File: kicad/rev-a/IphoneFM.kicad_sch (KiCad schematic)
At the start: 0 parts

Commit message: Step 1.4: U1 STM32U535CEUx placed; all 49 pins match netlist.json
Co-Authored-By: Claude Opus 5.5 <noreply@anthropic.com>
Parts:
- added U1: STM32U535CEU6, Package_DFN_QFN:QFN-48-1EP_7x7mm_P0.5mm_EP5.6x5.6mm, symbol MCU_ST_STM32U5:STM32U535CEUx
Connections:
- new net: U1.23 (VSS), U1.35 (VSS), U1.47 (VSS), U1.49 (VSS)
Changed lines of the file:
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@@
 		(comment 2 "Source of truth: design/rev-a/netlist.json")
+	)
+	(symbol
+		(lib_id "MCU_ST_STM32U5:STM32U535CEUx")
+		(at 223.52 251.46 0)
+		(unit 1)
+		(exclude_from_sim no)
+		(in_bom yes)
+		(on_board yes)
+		(dnp no)
+		(property "Reference" "U1"
+			(at 223.52 247.65 0)
+			(effects (font (size 1.27 1.27)))
+		)
+		(property "Value" "STM32U535CEU6"
+			(at 223.52 255.27 0)
+			(effects (font (size 1.27 1.27)))
+		)
+		(property "Footprint" "Package_DFN_QFN:QFN-48-1EP_7x7mm_P0.5mm_EP5.6x5.6mm"
+			(at 223.52 251.46 0)
+			(effects (font (size 1.27 1.27)) (hide yes))
+		)
+		(property "Datasheet" "~"
+			(at 223.52 251.46 0)
+			(effects (font (size 1.27 1.27)) (hide yes))
+		)
+		(instances
+			(project "IphoneFM"
+				(path "/efee88c9-028d-4fdb-86e0-0a4145b330e1"
+					(reference "U1") (unit 1)
+				)
+			)
+		)
 	)
 	(sheet_instances

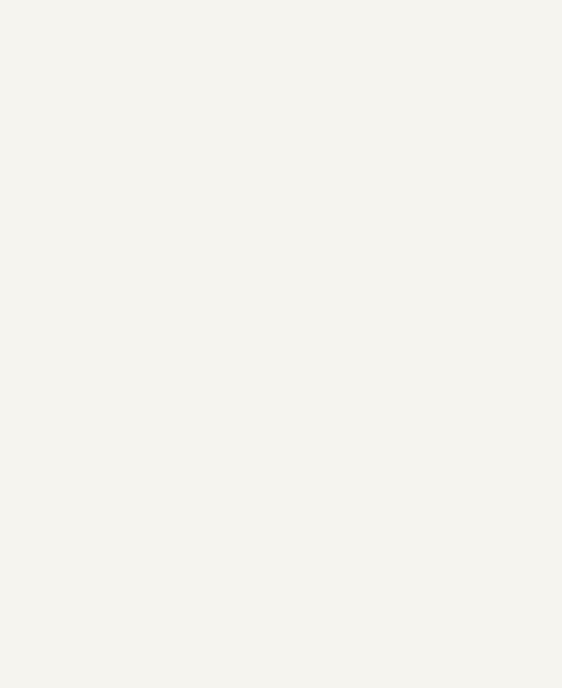
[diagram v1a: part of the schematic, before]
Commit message: Step 1.5: U2 LMX2571 placed from a project symbol built from SNAS654A p3-4 (tools/kicad_symbol.py)
Co-Authored-By: Claude Opus 5.5 <noreply@anthropic.com>
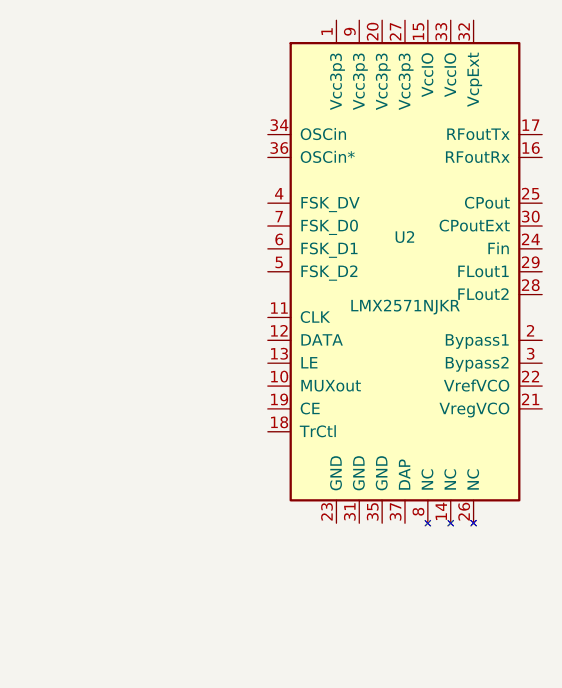
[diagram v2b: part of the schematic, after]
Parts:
- added U2: LMX2571NJKR, symbol IphoneFM:LMX2571
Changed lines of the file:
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@@
+		)
+	)
+	(symbol
+		(lib_id "IphoneFM:LMX2571")
+		(at 337.82 88.9 0)
+		(unit 1)
+		(exclude_from_sim no)
+		(in_bom yes)
+		(on_board yes)
+		(dnp no)
+		(property "Reference" "U2"
+			(at 337.82 85.09 0)
+			(effects (font (size 1.27 1.27)))
+		)
+		(property "Value" "LMX2571NJKR"
+			(at 337.82 92.71 0)
+			(effects (font (size 1.27 1.27)))
+		)
+		(property "Footprint" ""
+			(at 337.82 88.9 0)
+			(effects (font (size 1.27 1.27)) (hide yes))
+		)
+		(property "Datasheet" "~"
+			(at 337.82 88.9 0)
+			(effects (font (size 1.27 1.27)) (hide yes))
+		)
+		(instances
+			(project "IphoneFM"
+				(path "/efee88c9-028d-4fdb-86e0-0a4145b330e1"
+					(reference "U2") (unit 1)
+				)
+			)
 		)
 	)

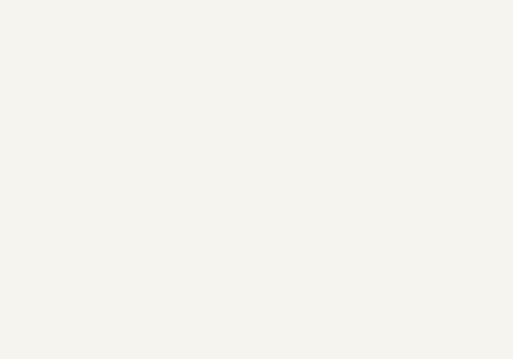
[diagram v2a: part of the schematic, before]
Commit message: Step 1.6: U3 AP2112K-3.3 placed (KiCad library symbol, 5/5 pins match)
Co-Authored-By: Claude Opus 5.5 <noreply@anthropic.com>
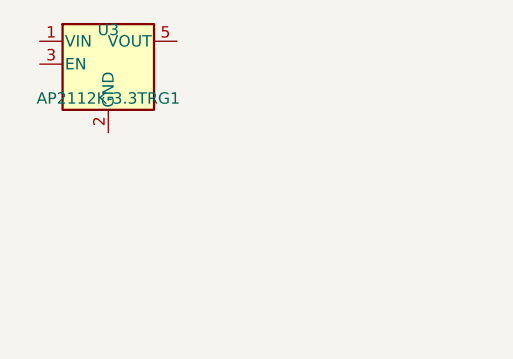
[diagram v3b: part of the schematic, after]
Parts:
- added U3: AP2112K-3.3TRG1, Package_TO_SOT_SMD:SOT-23-5, symbol Regulator_Linear:AP2112K-3.3
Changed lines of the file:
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@@
+		)
+	)
+	(symbol
+		(lib_id "Regulator_Linear:AP2112K-3.3")
+		(at 120.65 45.72 0)
+		(unit 1)
+		(exclude_from_sim no)
+		(in_bom yes)
+		(on_board yes)
+		(dnp no)
+		(property "Reference" "U3"
+			(at 120.65 41.91 0)
+			(effects (font (size 1.27 1.27)))
+		)
+		(property "Value" "AP2112K-3.3TRG1"
+			(at 120.65 49.53 0)
+			(effects (font (size 1.27 1.27)))
+		)
+		(property "Footprint" "Package_TO_SOT_SMD:SOT-23-5"
+			(at 120.65 45.72 0)
+			(effects (font (size 1.27 1.27)) (hide yes))
+		)
+		(property "Datasheet" "~"
+			(at 120.65 45.72 0)
+			(effects (font (size 1.27 1.27)) (hide yes))
+		)
+		(instances
+			(project "IphoneFM"
+				(path "/efee88c9-028d-4fdb-86e0-0a4145b330e1"
+					(reference "U3") (unit 1)
+				)
+			)
 		)
 	)

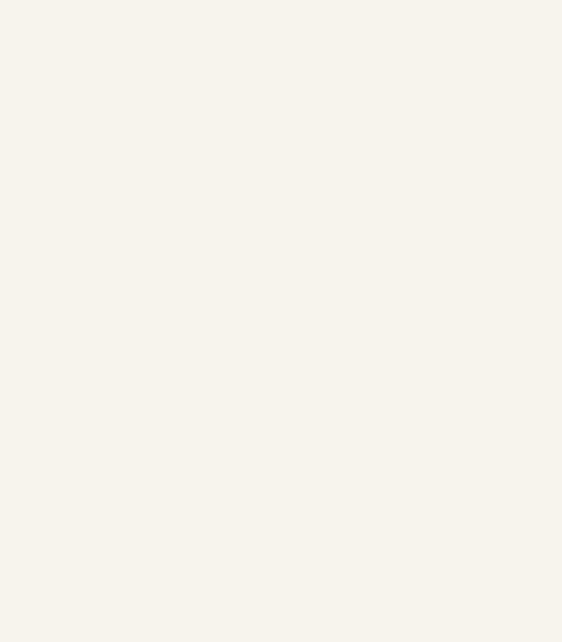
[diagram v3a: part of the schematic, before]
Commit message: Step 1.7: U4 Si4705-D60-GM placed from a project symbol (QFN-20, datasheet p16)
Co-Authored-By: Claude Opus 5.5 <noreply@anthropic.com>
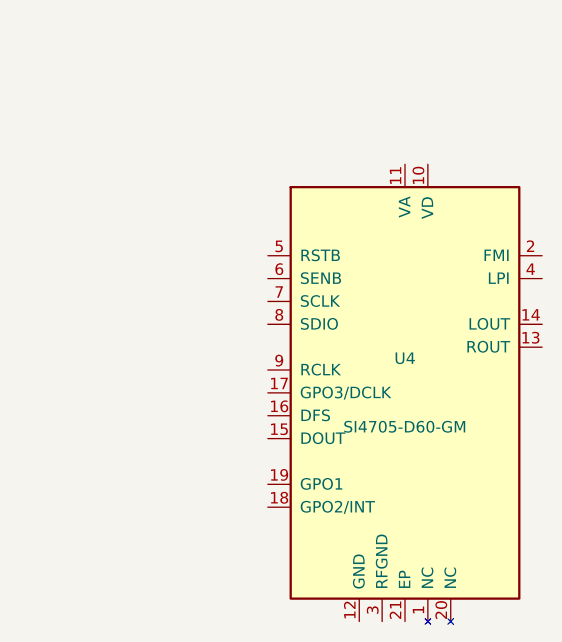
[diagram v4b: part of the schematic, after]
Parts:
- added U4: SI4705-D60-GM, symbol IphoneFM:Si4705-D60-GM
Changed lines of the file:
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@@
+		)
+	)
+	(symbol
+		(lib_id "IphoneFM:Si4705-D60-GM")
+		(at 365.76 304.8 0)
+		(unit 1)
+		(exclude_from_sim no)
+		(in_bom yes)
+		(on_board yes)
+		(dnp no)
+		(property "Reference" "U4"
+			(at 365.76 300.99 0)
+			(effects (font (size 1.27 1.27)))
+		)
+		(property "Value" "SI4705-D60-GM"
+			(at 365.76 308.61 0)
+			(effects (font (size 1.27 1.27)))
+		)
+		(property "Footprint" ""
+			(at 365.76 304.8 0)
+			(effects (font (size 1.27 1.27)) (hide yes))
+		)
+		(property "Datasheet" "~"
+			(at 365.76 304.8 0)
+			(effects (font (size 1.27 1.27)) (hide yes))
+		)
+		(instances
+			(project "IphoneFM"
+				(path "/efee88c9-028d-4fdb-86e0-0a4145b330e1"
+					(reference "U4") (unit 1)
+				)
+			)
 		)
 	)

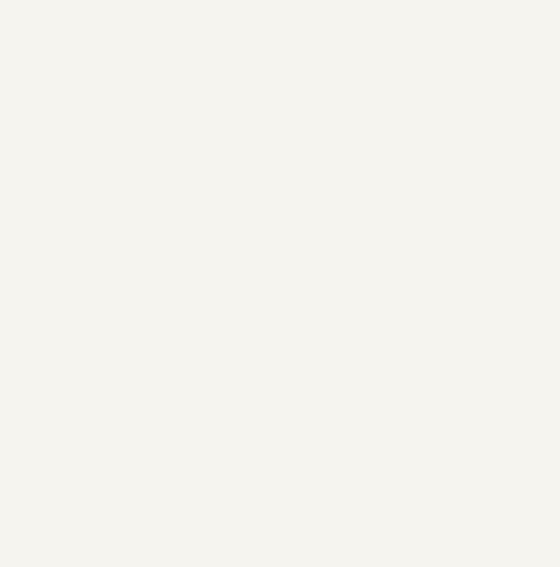
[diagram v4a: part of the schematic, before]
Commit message: Step 1.8: U5 PE42421 placed from a project symbol (p8)
Co-Authored-By: Claude Opus 5.5 <noreply@anthropic.com>
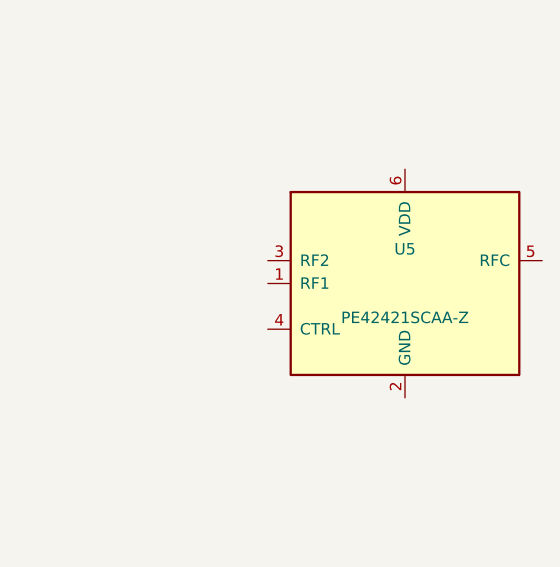
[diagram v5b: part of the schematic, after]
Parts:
- added U5: PE42421SCAA-Z, symbol IphoneFM:PE42421
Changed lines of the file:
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@@
+		)
+	)
+	(symbol
+		(lib_id "IphoneFM:PE42421")
+		(at 520.7 152.4 0)
+		(unit 1)
+		(exclude_from_sim no)
+		(in_bom yes)
+		(on_board yes)
+		(dnp no)
+		(property "Reference" "U5"
+			(at 520.7 148.59 0)
+			(effects (font (size 1.27 1.27)))
+		)
+		(property "Value" "PE42421SCAA-Z"
+			(at 520.7 156.21 0)
+			(effects (font (size 1.27 1.27)))
+		)
+		(property "Footprint" ""
+			(at 520.7 152.4 0)
+			(effects (font (size 1.27 1.27)) (hide yes))
+		)
+		(property "Datasheet" "~"
+			(at 520.7 152.4 0)
+			(effects (font (size 1.27 1.27)) (hide yes))
+		)
+		(instances
+			(project "IphoneFM"
+				(path "/efee88c9-028d-4fdb-86e0-0a4145b330e1"
+					(reference "U5") (unit 1)
+				)
+			)
 		)
 	)

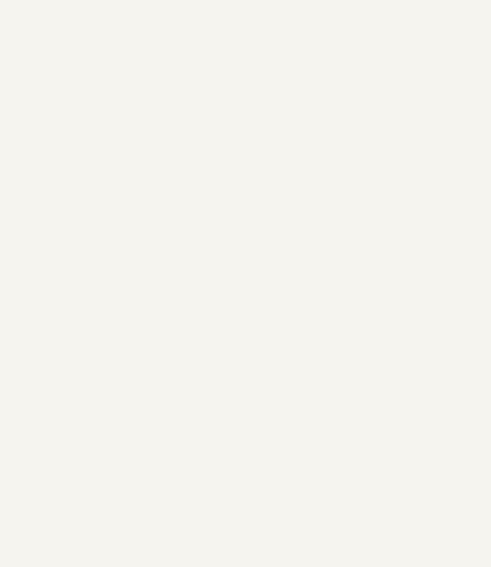
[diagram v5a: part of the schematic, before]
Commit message: Step 1.9: U6 USBLC6-2SC6 placed (KiCad library symbol, 6/6 pins match)
Co-Authored-By: Claude Opus 5.5 <noreply@anthropic.com>
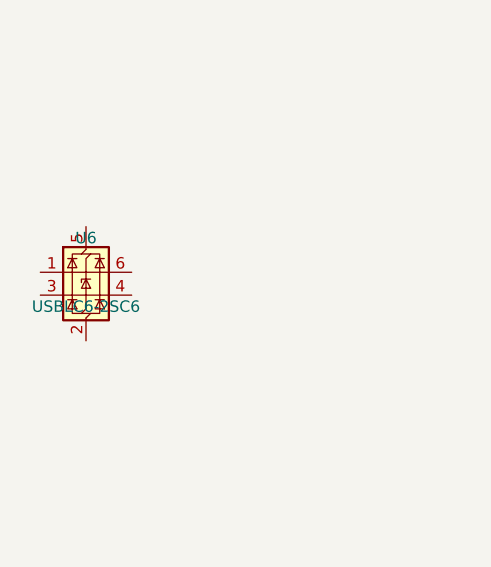
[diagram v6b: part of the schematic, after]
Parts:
- added U6: USBLC6-2SC6, Package_TO_SOT_SMD:SOT-23-6, symbol Power_Protection:USBLC6-2SC6
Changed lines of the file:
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@@
+		)
+	)
+	(symbol
+		(lib_id "Power_Protection:USBLC6-2SC6")
+		(at 73.66 93.98 0)
+		(unit 1)
+		(exclude_from_sim no)
+		(in_bom yes)
+		(on_board yes)
+		(dnp no)
+		(property "Reference" "U6"
+			(at 73.66 90.17 0)
+			(effects (font (size 1.27 1.27)))
+		)
+		(property "Value" "USBLC6-2SC6"
+			(at 73.66 97.79 0)
+			(effects (font (size 1.27 1.27)))
+		)
+		(property "Footprint" "Package_TO_SOT_SMD:SOT-23-6"
+			(at 73.66 93.98 0)
+			(effects (font (size 1.27 1.27)) (hide yes))
+		)
+		(property "Datasheet" "~"
+			(at 73.66 93.98 0)
+			(effects (font (size 1.27 1.27)) (hide yes))
+		)
+		(instances
+			(project "IphoneFM"
+				(path "/efee88c9-028d-4fdb-86e0-0a4145b330e1"
+					(reference "U6") (unit 1)
+				)
+			)
 		)
 	)

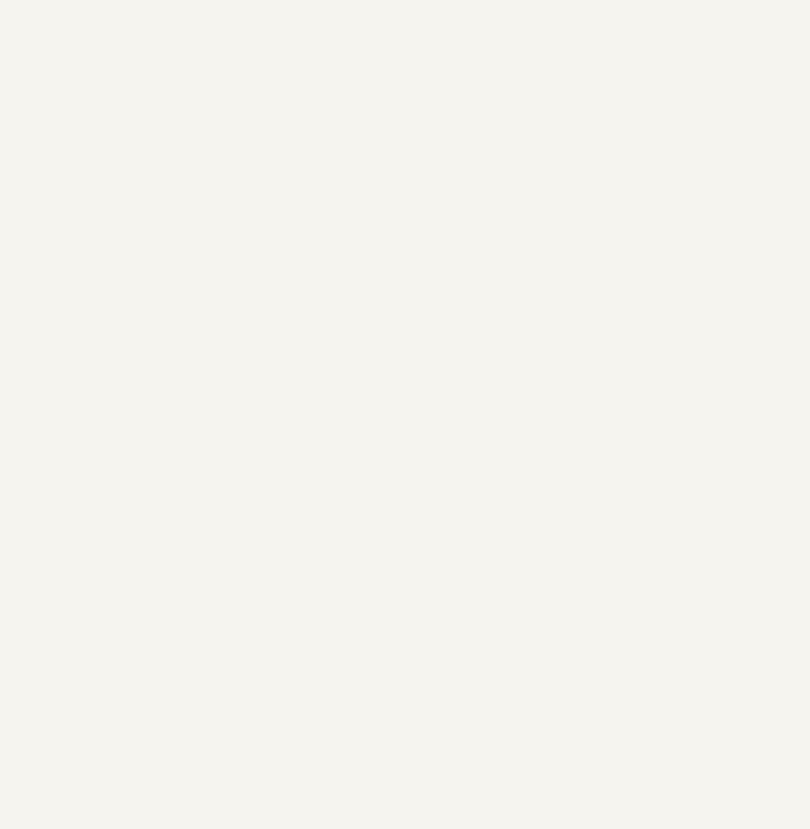
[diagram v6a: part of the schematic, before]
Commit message: Step 1.10: U7 PE43711 placed from a project symbol (Table 9 p28)
Co-Authored-By: Claude Opus 5.5 <noreply@anthropic.com>
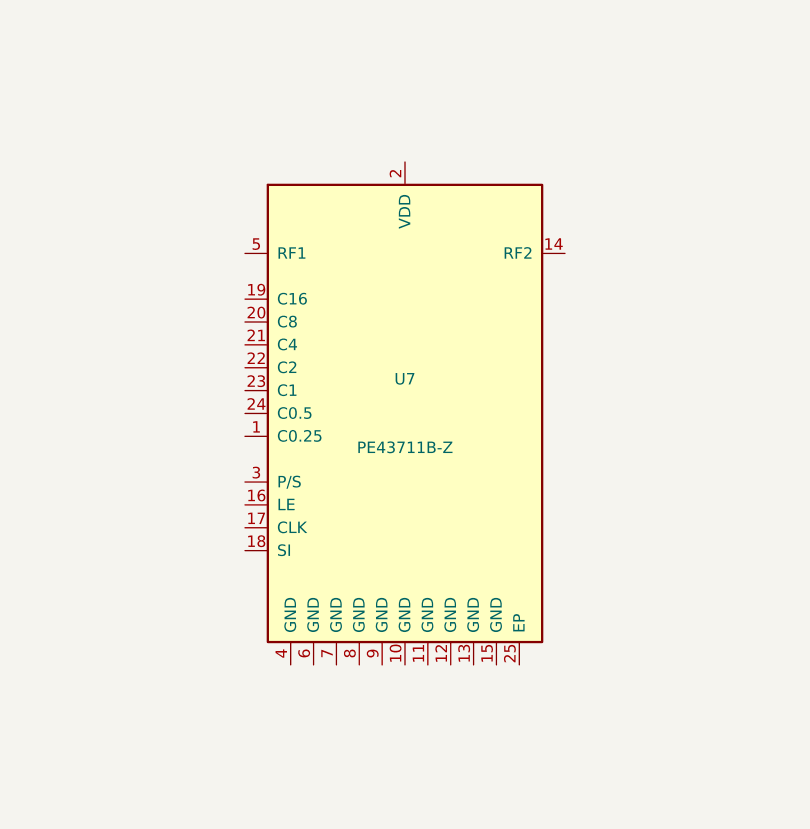
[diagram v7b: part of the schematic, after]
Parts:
- added U7: PE43711B-Z, symbol IphoneFM:PE43711
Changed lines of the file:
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@@
+		)
+	)
+	(symbol
+		(lib_id "IphoneFM:PE43711")
+		(at 406.4 101.6 0)
+		(unit 1)
+		(exclude_from_sim no)
+		(in_bom yes)
+		(on_board yes)
+		(dnp no)
+		(property "Reference" "U7"
+			(at 406.4 97.79 0)
+			(effects (font (size 1.27 1.27)))
+		)
+		(property "Value" "PE43711B-Z"
+			(at 406.4 105.41 0)
+			(effects (font (size 1.27 1.27)))
+		)
+		(property "Footprint" ""
+			(at 406.4 101.6 0)
+			(effects (font (size 1.27 1.27)) (hide yes))
+		)
+		(property "Datasheet" "~"
+			(at 406.4 101.6 0)
+			(effects (font (size 1.27 1.27)) (hide yes))
+		)
+		(instances
+			(project "IphoneFM"
+				(path "/efee88c9-028d-4fdb-86e0-0a4145b330e1"
+					(reference "U7") (unit 1)
+				)
+			)
 		)
 	)

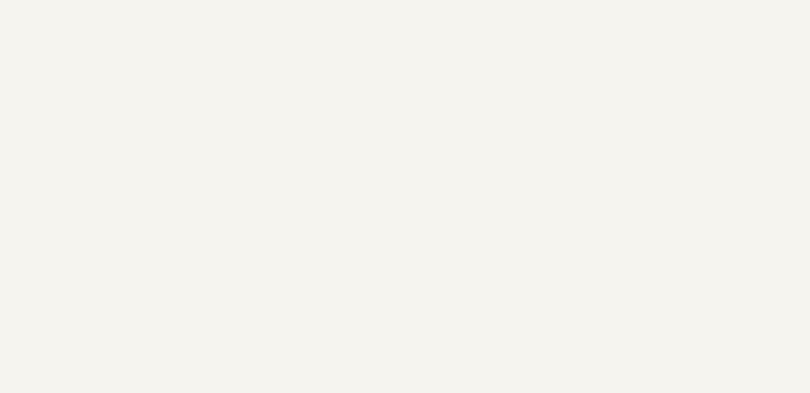
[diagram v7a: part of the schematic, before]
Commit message: Step 1.11: Y2 OT322520MJBA4SL 20 MHz placed from a project symbol (YSO110TR p2)
Co-Authored-By: Claude Opus 5.5 <noreply@anthropic.com>
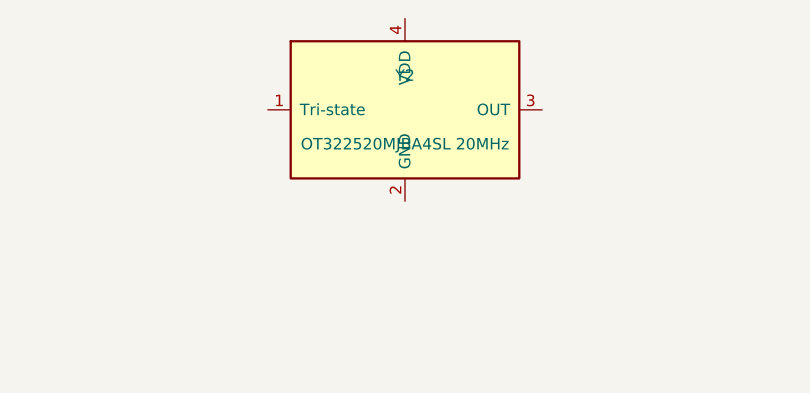
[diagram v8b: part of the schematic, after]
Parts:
- added Y2: OT322520MJBA4SL 20MHz, symbol IphoneFM:OT322520MJBA4SL
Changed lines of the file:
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@@
+		)
+	)
+	(symbol
+		(lib_id "IphoneFM:OT322520MJBA4SL")
+		(at 223.52 50.8 0)
+		(unit 1)
+		(exclude_from_sim no)
+		(in_bom yes)
+		(on_board yes)
+		(dnp no)
+		(property "Reference" "Y2"
+			(at 223.52 46.99 0)
+			(effects (font (size 1.27 1.27)))
+		)
+		(property "Value" "OT322520MJBA4SL 20MHz"
+			(at 223.52 54.61 0)
+			(effects (font (size 1.27 1.27)))
+		)
+		(property "Footprint" ""
+			(at 223.52 50.8 0)
+			(effects (font (size 1.27 1.27)) (hide yes))
+		)
+		(property "Datasheet" "~"
+			(at 223.52 50.8 0)
+			(effects (font (size 1.27 1.27)) (hide yes))
+		)
+		(instances
+			(project "IphoneFM"
+				(path "/efee88c9-028d-4fdb-86e0-0a4145b330e1"
+					(reference "Y2") (unit 1)
+				)
+			)
 		)
 	)
